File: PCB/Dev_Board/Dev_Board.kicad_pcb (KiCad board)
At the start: 2 copper layers, 50 x 50 mm, 40 parts, among them J1 USB_MICRO-B_FEMALE-SMT, Q1 16M, Q2 32.768k, SW1 TS342A2P, U1 AMS1117-3.3, U2 ATmega128RFR2

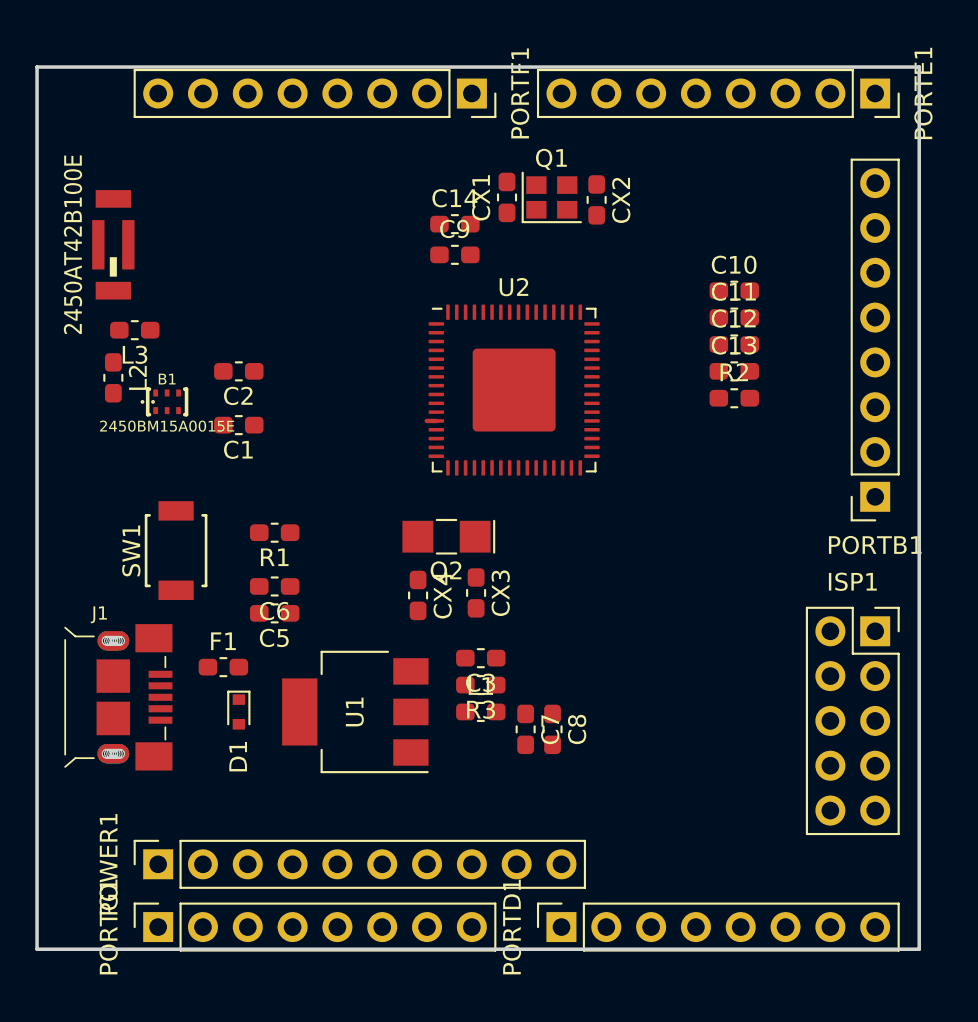
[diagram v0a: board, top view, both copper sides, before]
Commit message: Fixed L1 power net
Also added a power indicator LED
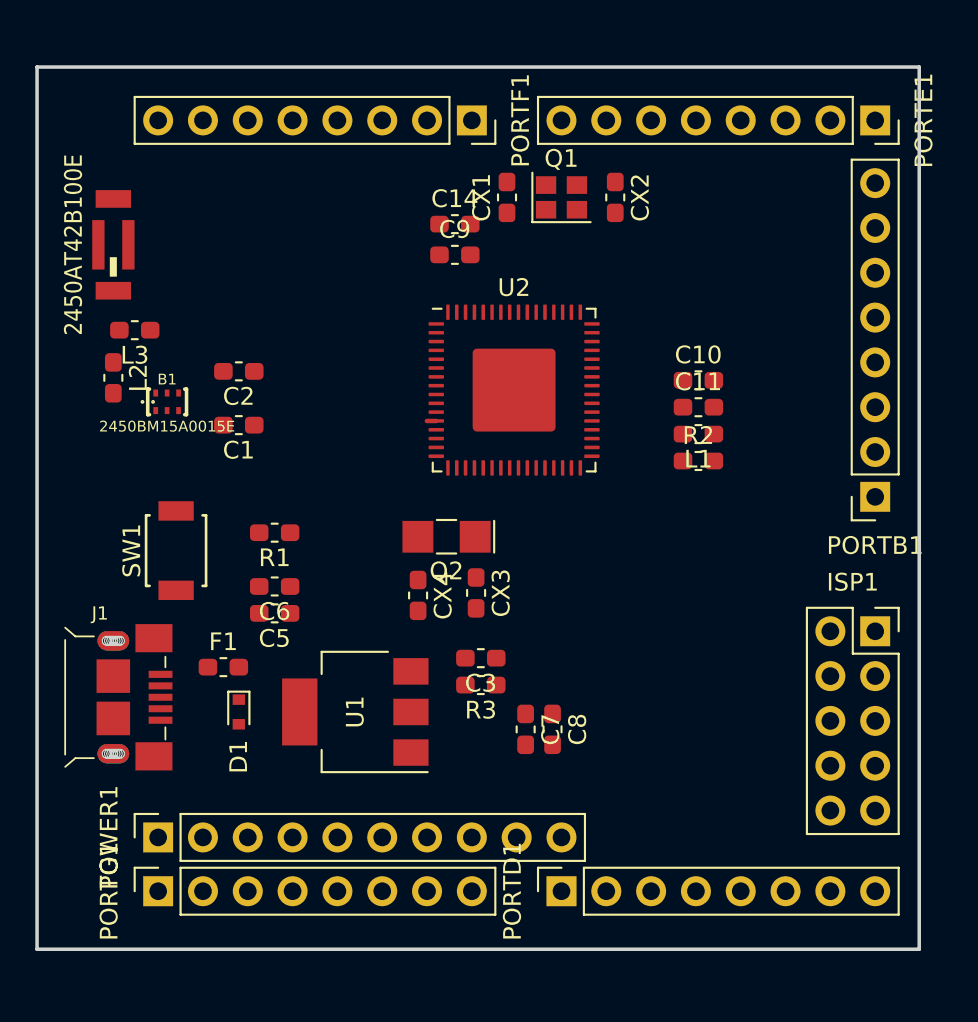
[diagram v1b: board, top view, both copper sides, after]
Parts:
- removed C12, C13: 100n, Capacitor_SMD:C_0603_1608Metric_Pad1.05x0.95mm_HandSolder
- moved L1 20.0 mm to (85.5, 82.8), turned to 180 degrees
- moved C10 5.47 mm to (85.5, 79.8)
- moved C11 5.47 mm to (85.5, 81.3)
- moved R2 4.10 mm to (85.5, 84.3)
- moved PORTD1 2.03 mm to (77.7, 108.7)
- moved PORTG1 2.03 mm to (54.9, 108.7)
- moved PORTE1 1.52 mm to (95.5, 65.0)
- moved PORTF1 1.52 mm to (72.6, 65.0)
- moved POWER1 1.52 mm to (54.9, 105.7)
- moved CX2 1.06 mm to (80.8, 69.4)
- moved Q1 0.55 mm to (77.7, 69.4)
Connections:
- C7 pad 1: +3V3 -> Net-(C7-Pad1)
- C8 pad 1: +3V3 -> Net-(C7-Pad1)
- L1 pad 1: Net-(L1-Pad1) -> Net-(C7-Pad1)
- U1 pad 2: Net-(L1-Pad1) -> Net-(C7-Pad1)

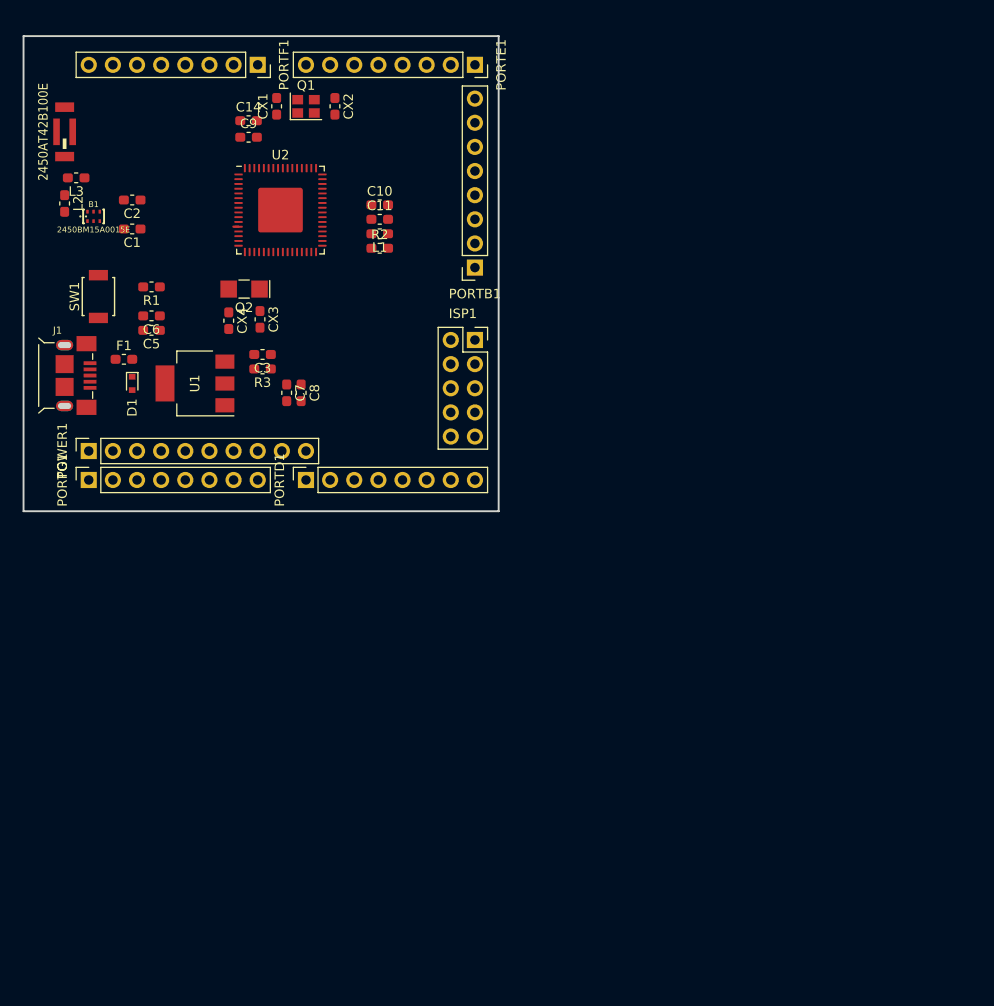
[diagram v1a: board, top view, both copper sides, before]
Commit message: Board design almost done
some parts need to be replaced with larger footprints(fuse, caps, etc...)
I haven't done the RF side yet.
Also, I changed the switch to similarly designed one that had more detailed dimensions.
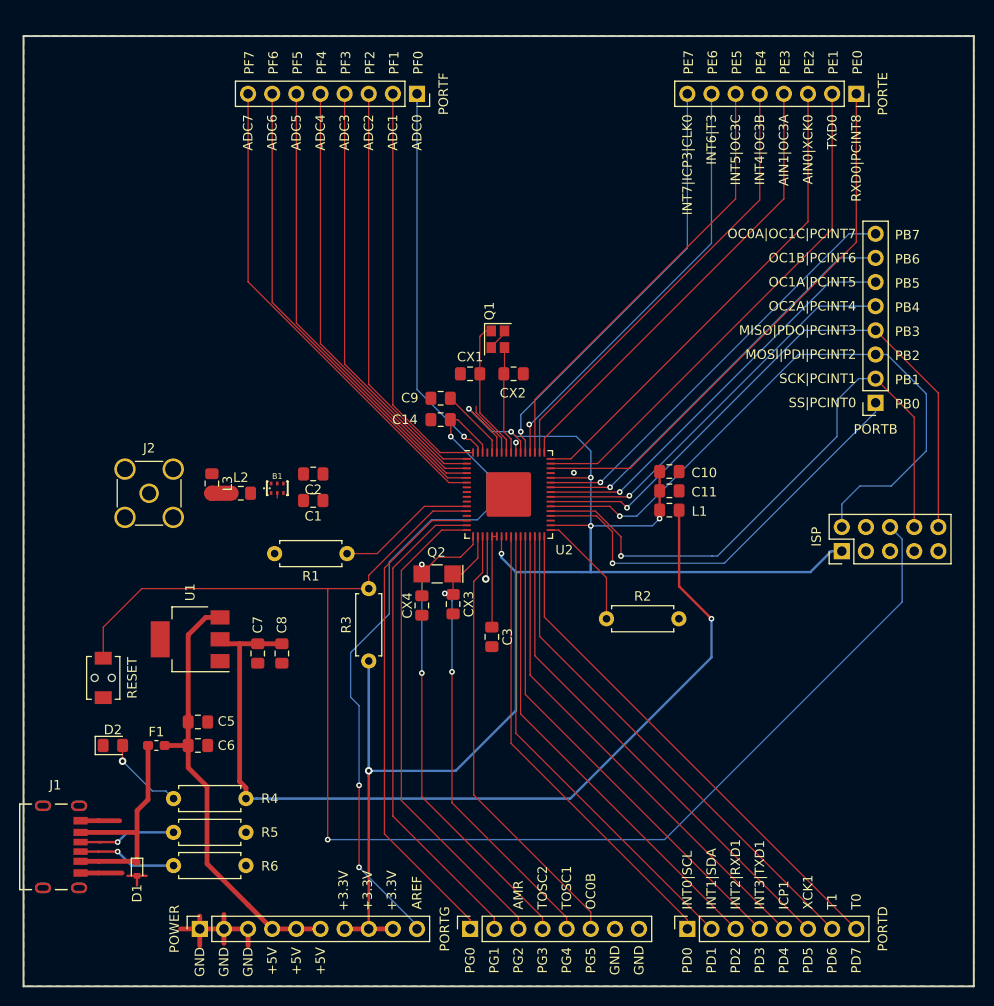
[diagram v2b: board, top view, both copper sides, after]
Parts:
- removed AE1: 2450AT42B100E, RFR2:2450AT42B100E
- added D2: E6C0603URAC1UDA, LED_SMD:LED_0805_2012Metric_Pad1.15x1.40mm_HandSolder, F.Cu at (57.4, 136.7)
- added J2: Conn_Coaxial, Connector_Coaxial:SMA_Amphenol_132134-11_Vertical, F.Cu at (61.2, 110.1)
- added R4: 56R, Resistor_THT:R_Axial_DIN0207_L6.3mm_D2.5mm_P7.62mm_Horizontal, F.Cu at (71.4, 142.2)
- added R5: 5.1k, Resistor_THT:R_Axial_DIN0207_L6.3mm_D2.5mm_P7.62mm_Horizontal, F.Cu at (71.4, 145.8)
- added R6: 5.1k, Resistor_THT:R_Axial_DIN0207_L6.3mm_D2.5mm_P7.62mm_Horizontal, F.Cu at (71.4, 149.3)
- C1, C10, C11, C14, C2, C3, C5, C6, C7, C8, C9, CX1, CX2, CX3, CX4: footprint Capacitor_SMD:C_0603_1608Metric_Pad1.05x0.95mm_HandSolder -> Capacitor_SMD:C_0805_2012Metric_Pad1.15x1.40mm_HandSolder
- ISP1: value Conn_02x05_Counter_Clockwise -> Conn_02x05_Odd_Even; footprint Connector_PinSocket_2.54mm:PinSocket_2x05_P2.54mm_Vertical -> Connector_PinHeader_2.54mm:PinHeader_2x05_P2.54mm_Vertical
- J1: value USB_MICRO-B_FEMALE-SMT -> TYPE-C-31-M-17; footprint RFR2:MCU-U52105 -> RFR2:TYPE-C-31-M-17
- L1, L2, L3: footprint Inductor_SMD:L_0603_1608Metric_Pad1.05x0.95mm_HandSolder -> Inductor_SMD:L_0805_2012Metric_Pad1.15x1.40mm_HandSolder
- R1, R2, R3: footprint Resistor_SMD:R_0603_1608Metric_Pad1.05x0.95mm_HandSolder -> Resistor_THT:R_Axial_DIN0207_L6.3mm_D2.5mm_P7.62mm_Horizontal
- SW1: value TS342A2P -> K2-1807SA-B4DW-06; footprint RFR2:TS342A2P -> RFR2:K2-1807SA-B4DW-06
- U2: value ATmega128RFR2 -> ATmega256RFR2
- moved PORTG1 62.0 mm to (95.0, 156.0)
- moved PORTD1 62.0 mm to (117.9, 156.0)
- moved POWER1 51.6 mm to (66.5, 156.0)
- moved D1 51.1 mm to (59.9, 149.7)
- moved J1 49.6 mm to (53.8, 147.3), turned to 270 degrees
- moved R2 45.7 mm to (109.3, 123.3)
- moved C6 45.5 mm to (66.4, 136.7), turned to 0 degrees
- moved ISP1 44.5 mm to (134.1, 116.2), turned to 90 degrees
- moved PORTB1 44.5 mm to (137.7, 100.6)
- moved L1 42.1 mm to (116.0, 111.9)
- moved C11 41.8 mm to (116.0, 109.9)
- moved C5 41.5 mm to (66.4, 134.2), turned to 0 degrees
- moved C10 41.4 mm to (116.0, 107.8)
- moved F1 40.8 mm to (62.0, 136.7)
- moved PORTE1 40.2 mm to (135.6, 68.1)
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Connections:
- D1 pad 1: +VDC -> +5V
- ISP1 pad 1: MOSI -> +3V3
- ISP1 pad 10: +3V3 -> MISO
- ISP1 pad 2: Net-(ISP1-Pad2) -> MOSI
- ISP1 pad 3: ~RST -> GND
- ISP1 pad 4: SCK -> Net-(ISP1-Pad4)
- ISP1 pad 5: MISO -> GND
- ISP1 pad 6: GND -> ~RST
- ISP1 pad 8: GND -> SCK
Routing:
- net +3V3: track 0.00 -> 162.5 mm, vias 0 -> 7
- net ~RST: track 0.54 -> 153.0 mm, vias 0 -> 1
- net Net-(C7-Pad1): track 0.00 -> 95.3 mm, vias 0 -> 1
- net AREF: track 0.00 -> 72.4 mm, vias 0 -> 3
- net MOSI: track 0.00 -> 68.4 mm, vias 0 -> 1
- net MISO: track 0.00 -> 65.6 mm, vias 0 -> 1
- net SCK: track 0.00 -> 64.7 mm, vias 0 -> 1
- net Net-(PORTE1-Pad1): track 0.00 -> 57.6 mm
- net Net-(PORTD1-Pad8): track 0.00 -> 54.9 mm
- net TOSC2: track 0.00 -> 54.5 mm, vias 0 -> 2
- net Net-(PORTE1-Pad2): track 0.00 -> 54.1 mm
- net Net-(PORTD1-Pad7): track 0.00 -> 54.1 mm
- net Net-(PORTD1-Pad6): track 0.00 -> 53.2 mm
- net Net-(PORTG1-Pad1): track 0.00 -> 52.4 mm
- net Net-(PORTD1-Pad5): track 0.00 -> 52.4 mm
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- added copper zone on B.Cu, net GND
- added copper zone on F.Cu, net GND
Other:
- board size 50 x 50 mm -> 100 x 100 mm
- net class CLOCK added: clearance 0.127, trace_width 0.127, via_dia 0.6, via_drill 0.3
- net class DIGITAL added: clearance 0.127, trace_width 0.127, via_dia 0.6, via_drill 0.3
- net class Default: clearance 0.2 -> 0.127; trace_width 0.25 -> 0.127; via_dia 0.8 -> 0.6; via_drill 0.4 -> 0.3
- net class MCU added: clearance 0.127, trace_width 0.127, via_dia 0.6, via_drill 0.3
- net class POWERLINE added: clearance 0.127, trace_width 0.508, via_dia 0.8, via_drill 0.4
- net class RF_100 added: clearance 0.127, trace_width 0.6731, via_dia 0.8, via_drill 0.4
- net class RF_50 added: clearance 0.127, trace_width 1.6002, via_dia 0.8, via_drill 0.4
- rule trace_clearance: 0.2 -> 0.127
- rule trace_min: 0.2 -> 0.0889
- rule via_min_drill: 0.3 -> 0.2
- rule via_min_size: 0.4 -> 0.45
- board text added: "+3.3V"
- board text added: "+5V"
- board text added: "ADC0"
- board text added: "ADC1"
- board text added: "ADC2"
- board text added: "ADC3"
- board text added: "ADC4"
- board text added: "ADC5"
- board text added: "ADC6"
- board text added: "ADC7"
- board text added: "AIN0|XCK0"
- board text added: "AIN1|OC3A"
- board text added: "AMR"
- board text added: "AREF"
- board text added: "GND"
- board text added: "ICP1"
- board text added: "INT0|SCL"
- board text added: "INT1|SDA"
- board text added: "INT2|RXD1"
- board text added: "INT3|TXD1"
- board text added: "INT4|OC3B"
- board text added: "INT5|OC3C"
- board text added: "INT6|T3"
- board text added: "INT7|ICP3|CLK0"
- board text added: "ISP"
- board text added: "MISO|PDO|PCINT3"
- board text added: "MOSI|PDI|PCINT2"
- board text added: "OC0A|OC1C|PCINT7"
- board text added: "OC0B"
- board text added: "OC1A|PCINT5"
- board text added: "OC1B|PCINT6"
- board text added: "OC2A|PCINT4"
- board text added: "PB0"
- board text added: "PB1"
- board text added: "PB2"
- board text added: "PB3"
- board text added: "PB4"
- board text added: "PB5"
- board text added: "PB6"
- board text added: "PB7"
- board text added: "PD0"
- board text added: "PD1"
- board text added: "PD2"
- board text added: "PD3"
- board text added: "PD4"
- board text added: "PD5"
- board text added: "PD6"
- board text added: "PD7"
- board text added: "PE0"
- board text added: "PE1"
- board text added: "PE2"
- board text added: "PE3"
- board text added: "PE4"
- board text added: "PE5"
- board text added: "PE6"
- board text added: "PE7"
- board text added: "PF0"
- board text added: "PF1"
- board text added: "PF2"
- board text added: "PF3"
- board text added: "PF4"
- board text added: "PF5"
- board text added: "PF6"
- board text added: "PF7"
- board text added: "PG0"
- board text added: "PG1"
- board text added: "PG2"
- board text added: "PG3"
- board text added: "PG4"
- board text added: "PG5"
- board text added: "PORTB"
- board text added: "PORTD"
- board text added: "PORTE"
- board text added: "PORTF"
- board text added: "PORTG"
- board text added: "POWER"
- board text added: "RESET"
- board text added: "RXD0|PCINT8"
- board text added: "SCK|PCINT1"
- board text added: "SS|PCINT0"
- board text added: "T0"
- board text added: "T1"
- board text added: "TOSC1"
- board text added: "TOSC2"
- board text added: "TXD0"
- board text added: "XCK1"

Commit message: Final PCB design
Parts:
- B1: value 2450BM15A0015E -> BALUN0805; footprint RFR2:BALUN-0805 -> RFR2:2450BM15A0015E
- F1: value MF-FSMF050X-2 -> MF-NSMF110-2; footprint Fuse:Fuse_0603_1608Metric_Pad1.05x0.95mm_HandSolder -> Fuse:Fuse_1206_3216Metric_Pad1.42x1.75mm_HandSolder
- J2: footprint Connector_Coaxial:SMA_Amphenol_132134-11_Vertical -> RFR2:U.FL
- L1, L3: footprint Inductor_SMD:L_0805_2012Metric_Pad1.15x1.40mm_HandSolder -> Inductor_SMD:L_0603_1608Metric_Pad1.05x0.95mm_HandSolder
- moved R1 18.0 mm to (81.7, 134.5)
- moved L3 1.72 mm to (66.5, 110.2)
- moved J2 1.08 mm to (61.7, 111.1), turned to 90 degrees
- moved F1 1.02 mm to (62.0, 135.6), turned to 90 degrees
- moved L2 0.95 mm to (70.9, 111.1)
- moved C1 0.83 mm to (78.5, 111.7)
- moved B1 0.70 mm to (74.7, 110.3), turned to 90 degrees
- moved C2 0.70 mm to (78.5, 108.8)
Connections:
- C1 pad 2: Net-(B1-Pad3) -> Net-(B1-PadBAL1)
- C2 pad 2: Net-(B1-Pad4) -> Net-(B1-PadBAL2)
- L2 pad 2: Net-(B1-Pad1) -> Net-(B1-PadUNBAL)
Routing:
- net GND: track 40.7 -> 62.2 mm, vias 3 -> 231
- net Net-(R1-Pad1): track 14.7 -> 33.0 mm, vias 0 -> 1
- net RF_P: track 0.00 -> 15.6 mm
- net RF_N: track 0.00 -> 15.6 mm
- net Net-(J2-Pad1): track 2.03 -> 6.64 mm
- net Net-(B1-PadBAL2): track 0.00 -> 3.49 mm
- net Net-(B1-PadBAL1): track 0.00 -> 3.32 mm
- net Net-(B1-PadUNBAL): track 0.00 -> 2.17 mm
- net +VDC: track 46.5 -> 47.4 mm
- added copper zone on F.Cu, net RF_N
- added copper zone on F.Cu, net RF_P
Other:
- net class RF_100: trace_width 0.6731 -> 0.6604
- net class RF_50: trace_width 1.6002 -> 0.3556
- board text added: "ATmega64/128/256RFR2 Development Board"
- board text added: "Design by RiTA* Quipu 2019"
